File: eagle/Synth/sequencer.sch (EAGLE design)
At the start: 21 parts, among them U1 ATMEGA328P_PDIP, Y1 16MHz

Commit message: new stuff
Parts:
- added IC1: LM555N, adafruit:LM555N
- added T1, T2: 2N2222, adafruit:2N2222
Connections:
- new net N$2: T1.B, T2.B
- net GND: now also T1.E, T2.E
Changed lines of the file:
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@@
 <grid distance="0.1" unitdist="inch" unit="inch" style="lines" multiple="1" display="no" altdistance="0.01" altunitdist="inch" altunit="inch"/>
 <layers>
-<layer number="1" name="Top" color="4" fill="1" visible="yes" active="no"/>
-<layer number="16" name="Bottom" color="1" fill="1" visible="yes" active="no"/>
-<layer number="17" name="Pads" color="2" fill="1" visible="yes" active="no"/>
-<layer number="18" name="Vias" color="2" fill="1" visible="yes" active="no"/>
-<layer number="19" name="Unrouted" color="6" fill="1" visible="yes" active="no"/>
-<layer number="20" name="Dimension" color="15" fill="1" visible="yes" active="no"/>
-<layer number="21" name="tPlace" color="7" fill="1" visible="yes" active="no"/>
-<layer number="22" name="bPlace" color="7" fill="1" visible="yes" active="no"/>
-<layer number="23" name="tOrigins" color="15" fill="1" visible="yes" active="no"/>
-<layer number="24" name="bOrigins" color="15" fill="1" visible="yes" active="no"/>
-<layer number="25" name="tNames" color="7" fill="1" visible="yes" active="no"/>
-<layer number="26" name="bNames" color="7" fill="1" visible="yes" active="no"/>
-<layer number="27" name="tValues" color="7" fill="1" visible="yes" active="no"/>
-<layer number="28" name="bValues" color="7" fill="1" visible="yes" active="no"/>
+<layer number="1" name="Top" color="4" fill="1" visible="no" active="no"/>
+<layer number="16" name="Bottom" color="1" fill="1" visible="no" active="no"/>
+<layer number="17" name="Pads" color="2" fill="1" visible="no" active="no"/>
+<layer number="18" name="Vias" color="2" fill="1" visible="no" active="no"/>
+<layer number="19" name="Unrouted" color="6" fill="1" visible="no" active="no"/>
+<layer number="20" name="Dimension" color="15" fill="1" visible="no" active="no"/>
+<layer number="21" name="tPlace" color="7" fill="1" visible="no" active="no"/>
+<layer number="22" name="bPlace" color="7" fill="1" visible="no" active="no"/>
+<layer number="23" name="tOrigins" color="15" fill="1" visible="no" active="no"/>
+<layer number="24" name="bOrigins" color="15" fill="1" visible="no" active="no"/>
+<layer number="25" name="tNames" color="7" fill="1" visible="no" active="no"/>
+<layer number="26" name="bNames" color="7" fill="1" visible="no" active="no"/>
+<layer number="27" name="tValues" color="7" fill="1" visible="no" active="no"/>
+<layer number="28" name="bValues" color="7" fill="1" visible="no" active="no"/>
 <layer number="29" name="tStop" color="7" fill="3" visible="no" active="no"/>
 <layer number="30" name="bStop" color="7" fill="6" visible="no" active="no"/>
@@
 <layer number="35" name="tGlue" color="7" fill="4" visible="no" active="no"/>
 <layer number="36" name="bGlue" color="7" fill="5" visible="no" active="no"/>
-<layer number="37" name="tTest" color="7" fill="1" visible="yes" active="no"/>
-<layer number="38" name="bTest" color="7" fill="1" visible="yes" active="no"/>
+<layer number="37" name="tTest" color="7" fill="1" visible="no" active="no"/>
+<layer number="38" name="bTest" color="7" fill="1" visible="no" active="no"/>
 <layer number="39" name="tKeepout" color="4" fill="11" visible="no" active="no"/>
 <layer number="40" name="bKeepout" color="1" fill="11" visible="no" active="no"/>
@@
 <layer number="44" name="Drills" color="7" fill="1" visible="no" active="no"/>
 <layer number="45" name="Holes" color="7" fill="1" visible="no" active="no"/>
-<layer number="46" name="Milling" color="3" fill="1" visible="yes" active="no"/>
-<layer number="47" name="Measures" color="7" fill="1" visible="yes" active="no"/>
-<layer number="48" name="Document" color="7" fill="1" visible="yes" active="no"/>
-<layer number="49" name="Reference" color="7" fill="1" visible="yes" active="no"/>
-<layer number="50" name="dxf" color="7" fill="1" visible="yes" active="no"/>
-<layer number="51" name="tDocu" color="7" fill="1" visible="yes" active="no"/>
-<layer number="52" name="bDocu" color="7" fill="1" visible="yes" active="no"/>
-<layer number="53" name="tGND_GNDA" color="7" fill="9" visible="yes" active="no"/>
-<layer number="54" name="bGND_GNDA" color="1" fill="9" visible="yes" active="no"/>
-<layer number="56" name="wert" color="7" fill="1" visible="yes" active="no"/>
-<layer number="57" name="tCAD" color="7" fill="1" visible="yes" active="no"/>
-<layer number="59" name="tCarbon" color="7" fill="1" visible="yes" active="no"/>
-<layer number="60" name="bCarbon" color="7" fill="1" visible="yes" active="no"/>
+<layer number="46" name="Milling" color="3" fill="1" visible="no" active="no"/>
+<layer number="47" name="Measures" color="7" fill="1" visible="no" active="no"/>
+<layer number="48" name="Document" color="7" fill="1" visible="no" active="no"/>
+<layer number="49" name="Reference" color="7" fill="1" visible="no" active="no"/>
+<layer number="50" name="dxf" color="7" fill="1" visible="no" active="no"/>
+<layer number="51" name="tDocu" color="7" fill="1" visible="no" active="no"/>
+<layer number="52" name="bDocu" color="7" fill="1" visible="no" active="no"/>
+<layer number="53" name="tGND_GNDA" color="7" fill="9" visible="no" active="no"/>
+<layer number="54" name="bGND_GNDA" color="1" fill="9" visible="no" active="no"/>
+<layer number="56" name="wert" color="7" fill="1" visible="no" active="no"/>
+<layer number="57" name="tCAD" color="7" fill="1" visible="no" active="no"/>
+<layer number="59" name="tCarbon" color="7" fill="1" visible="no" active="no"/>
+<layer number="60" name="bCarbon" color="7" fill="1" visible="no" active="no"/>
 <layer number="90" name="Modules" color="5" fill="1" visible="yes" active="yes"/>
 <layer number="91" name="Nets" color="2" fill="1" visible="yes" active="yes"/>
@@
 <part name="S1" library="switch" deviceset="TL36YO" device="" value="TRIGGER_MODE"/>
 <part name="S2" library="switch" deviceset="TL36YO" device="" value="REVERSE"/>
+<part name="IC1" library="adafruit" deviceset="*555" device="N" technology="LM"/>
+<part name="T1" library="adafruit" deviceset="2N2222" device=""/>
+<part name="T2" library="adafruit" deviceset="2N2222" device=""/>
+<part name="GND13" library="supply1" deviceset="GND" device=""/>
 </parts>
 <sheets>
@@
 <instance part="S1" gate="BEF1" x="124.46" y="160.02"/>
 <instance part="S2" gate="BEF1" x="139.7" y="160.02"/>
+<instance part="IC1" gate="A" x="25.4" y="43.18"/>
+<instance part="T1" gate="G$1" x="66.04" y="66.04"/>
+<instance part="T2" gate="G$1" x="45.72" y="66.04" rot="MR0"/>
+<instance part="GND13" gate="1" x="55.88" y="53.34"/>
 </instances>
 <busses>
@@
 <pinref part="C2" gate="G$1" pin="2"/>
 <wire x1="35.56" y1="129.54" x2="35.56" y2="134.62" width="0.1524" layer="91"/>
+</segment>
+<segment>
+<pinref part="T2" gate="G$1" pin="E"/>
+<wire x1="43.18" y1="60.96" x2="43.18" y2="55.88" width="0.1524" layer="91"/>
+<pinref part="T1" gate="G$1" pin="E"/>
+<wire x1="43.18" y1="55.88" x2="55.88" y2="55.88" width="0.1524" layer="91"/>
+<wire x1="55.88" y1="55.88" x2="68.58" y2="55.88" width="0.1524" layer="91"/>
+<wire x1="68.58" y1="55.88" x2="68.58" y2="60.96" width="0.1524" layer="91"/>
+<pinref part="GND13" gate="1" pin="GND"/>
+<junction x="55.88" y="55.88"/>
 </segment>
 </net>
@@
 </segment>
 </net>
+<net name="N$2" class="0">
+<segment>
+<pinref part="T2" gate="G$1" pin="B"/>
+<pinref part="T1" gate="G$1" pin="B"/>
+<wire x1="48.26" y1="66.04" x2="63.5" y2="66.04" width="0.1524" layer="91"/>
+</segment>
+</net>

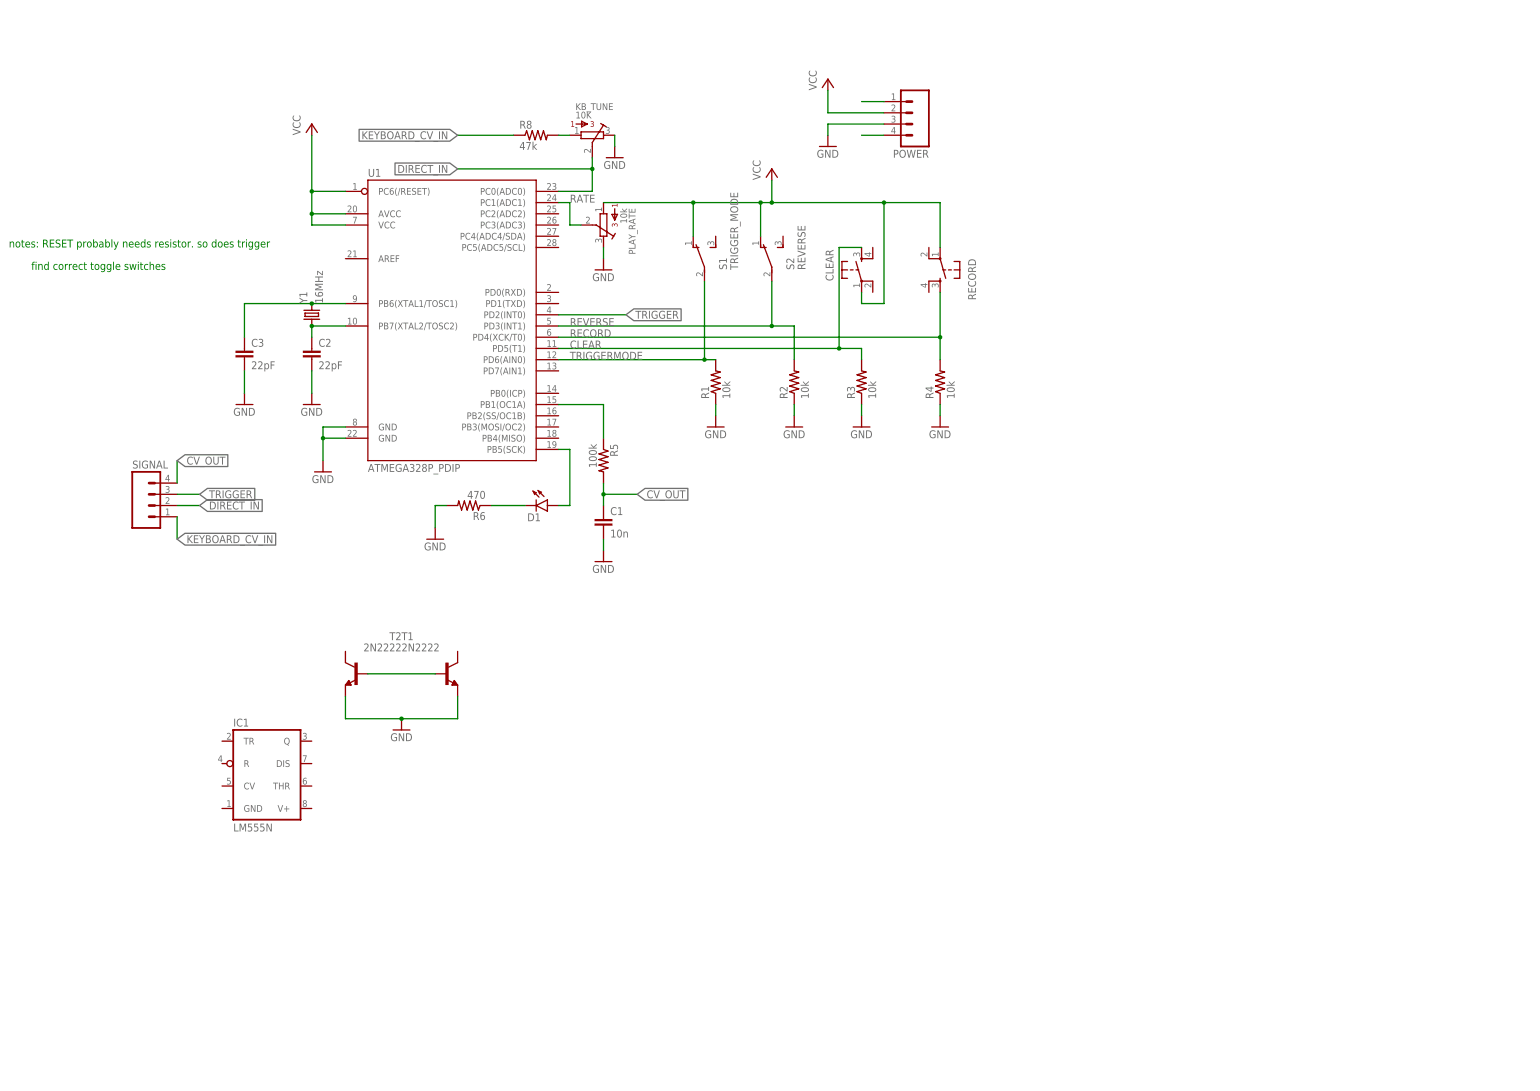
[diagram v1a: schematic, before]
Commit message: added ADC, cleaned up schematic
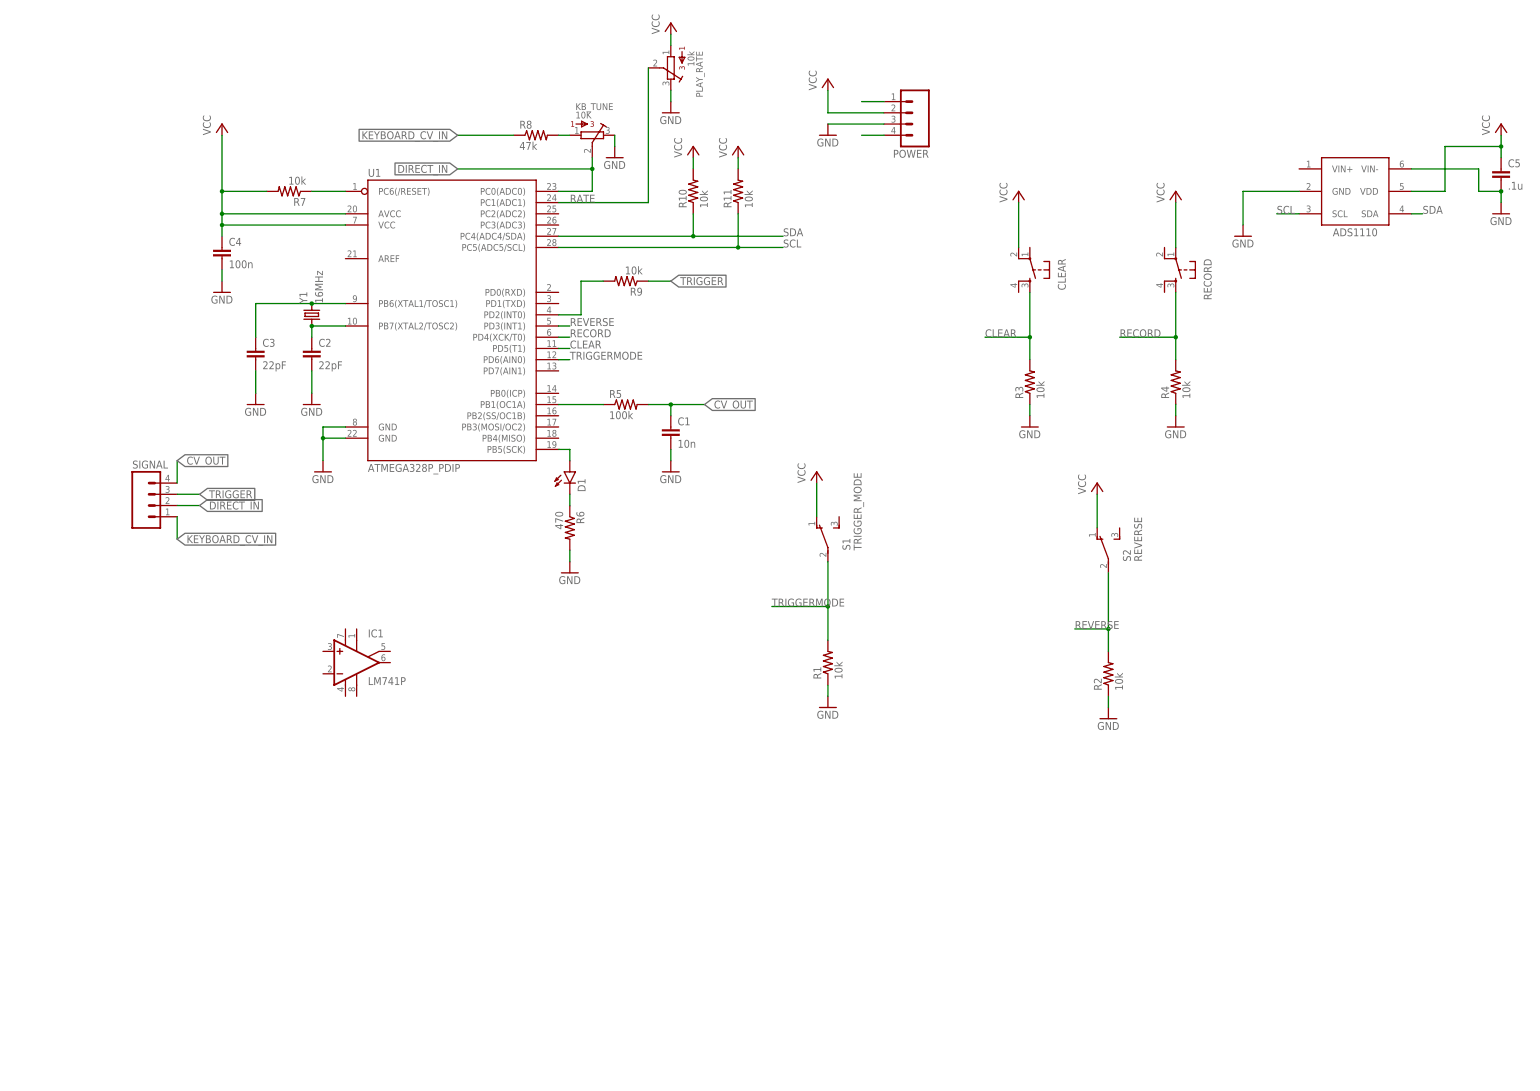
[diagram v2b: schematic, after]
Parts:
- removed T1, T2: 2N2222, adafruit:2N2222
- added C4: 100n, SparkFun-Capacitors:CAP1206
- added C5: .1u, SparkFun-Capacitors:CAP1206
- added IC2: (no value), ads11xx:ADS1110
- added R10, R11, R7, R9: 10k, SparkFun-Passives:RESISTOR1206
- IC1: value LM555N -> LM741P; device adafruit:LM555N -> linear:LM741P
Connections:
- new net N$10: U1.PD3(INT1)
- new net N$12: R9.2, U1.PD2(INT0)
- new net N$5: R7.1, U1.PC6(/RESET)
- new net N$9: U1.PD4(XCK/T0)
- new net SCL: IC2.SCL, R11.1, U1.PC5(ADC5/SCL)
- new net SDA: IC2.SDA, R10.1, U1.PC4(ADC4/SDA)
- net GND: now also C4.2, C5.2, IC2.GND, IC2.VIN-; no longer T1.E, T2.E
- net N$2: now also U1.PD6(AIN0); no longer T1.B, T2.B
- net RECORD: no longer U1.PD4(XCK/T0)
- net REVERSE: no longer U1.PD3(INT1)
- net TRIGGER: now also R9.1; no longer U1.PD2(INT0)
- net TRIGGERMODE: no longer U1.PD6(AIN0)
- net VCC: now also C4.1, C5.1, CLEAR.2, IC2.VDD, R10.2, R11.2, R7.2; no longer CLEAR.1, U1.PC6(/RESET)
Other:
- note removed: "find correct toggle switches"
- note removed: "notes: RESET probably needs resistor. so does trigger"
- moved on the sheet: C1, C3, CLEAR, D1, PLAY_RATE, R1, R2, R3, R4, R5, R6, RECORD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

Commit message: uncommited board changes
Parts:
- added C6: 1u, SparkFun-Capacitors:CAP1206
- added C7: 10UF-25V-10%(SMT-TANT), SparkFun-Capacitors:10UF-25V-10%(SMT-TANT)
- added R12, R13, R14, R15, R16: 100k, SparkFun-Passives:RESISTOR1206
- added R17: 680\, SparkFun-Passives:RESISTOR1206
- added RATE: 100K, SparkFun-Electromechanical:POTALPS-KIT
- added U2: MAX5217GUA+, cjk:MAX5217GUA+
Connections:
- new net N$13: IC1.+IN, R12.1, R13.1, R14.2
- new net N$15: R17.2, RATE.A
- new net N$17: C6.2, C7.+, R15.1, R16.2
- new net N$18: C6.1, IC1.-IN, R17.1
- new net N$19: IC1.OUT, R12.2, RATE.E, RATE.S
- net GND: now also C7.-, R14.1, R16.1, U2.*AUX, U2.ADDR, U2.GND
- net SCL: now also U2.SCL
- net SDA: now also U2.SDA
- net VCC: now also IC1.V+, R13.2, R15.2, U2.REF, U2.VDD
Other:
- moved on the sheet: C5, IC1

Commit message: updated sequencer eagle files for current version
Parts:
- removed PLAY_RATE: 10k, bourns:3386-P
- removed SIGNAL: (no value), SparkFun-Connectors:M04PTH
- added IO: HEADER-06X1-FEMALE, GeekAmmo:HEADER-06X1-FEMALE
- added R18, R20: 10k, SparkFun-Passives:RESISTOR1206
- added R19: 220???, SparkFun-Passives:RESISTOR1206
- added S3: RATE_SRC, switch:TL36YO
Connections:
- removed net N$10: U1.PD3(INT1)
- removed net N$12: R9.2, U1.PD2(INT0)
- removed net N$19: IC1.OUT, R12.2, RATE.E, RATE.S
- removed net N$9: U1.PD4(XCK/T0)
- new net PLAYBACKGATE: IO.1, R20.2, U1.PB0(ICP)
- new net RATE_EXTERNAL: IO.2, S3.S
- new net RATE_INTERNAL: IC1.OUT, R12.2, RATE.E, RATE.S, S3.O
- net CLEAR: now also U1.PD6(AIN0); no longer U1.PD5(T1)
- net CV_OUT: now also IO.6; no longer SIGNAL.4
- net DIRECT_IN: now also IO.4; no longer SIGNAL.2
- net GND: now also R18.1, R19.1, R20.1, R9.1; no longer KB_TUNE.3, PLAY_RATE.3
- net KEYBOARD_CV_IN: now also IO.5; no longer SIGNAL.1
- net N$2: now also KB_TUNE.3, R19.2; no longer U1.PD6(AIN0)
- net RATE: now also R18.2, S3.P, U1.PD2(INT0); no longer PLAY_RATE.2, U1.PC1(ADC1)
- net RECORD: now also U1.PD5(T1)
- net REVERSE: now also U1.PD4(XCK/T0)
- net TRIGGER: now also IO.3, R9.2, U1.PD3(INT1); no longer R9.1, SIGNAL.3
- net TRIGGERMODE: now also U1.PD7(AIN1)
- net VCC: no longer PLAY_RATE.1
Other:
- note added: "16-bit ADC"
- note added: "16-bit DAC"
- note added: "INTERNAL_CLOCK"
- moved on the sheet: C1, C5, C6, C7, CLEAR, IC1, POWER, R1, R12, R13, R14, R15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
